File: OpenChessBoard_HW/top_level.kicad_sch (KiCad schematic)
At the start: 25 parts, among them U1 AH3572-SA-7, U2 AH3572-SA-7, U3 AH3572-SA-7, U4 AH3572-SA-7, U5 74HC4051, U6 74LVC1G79

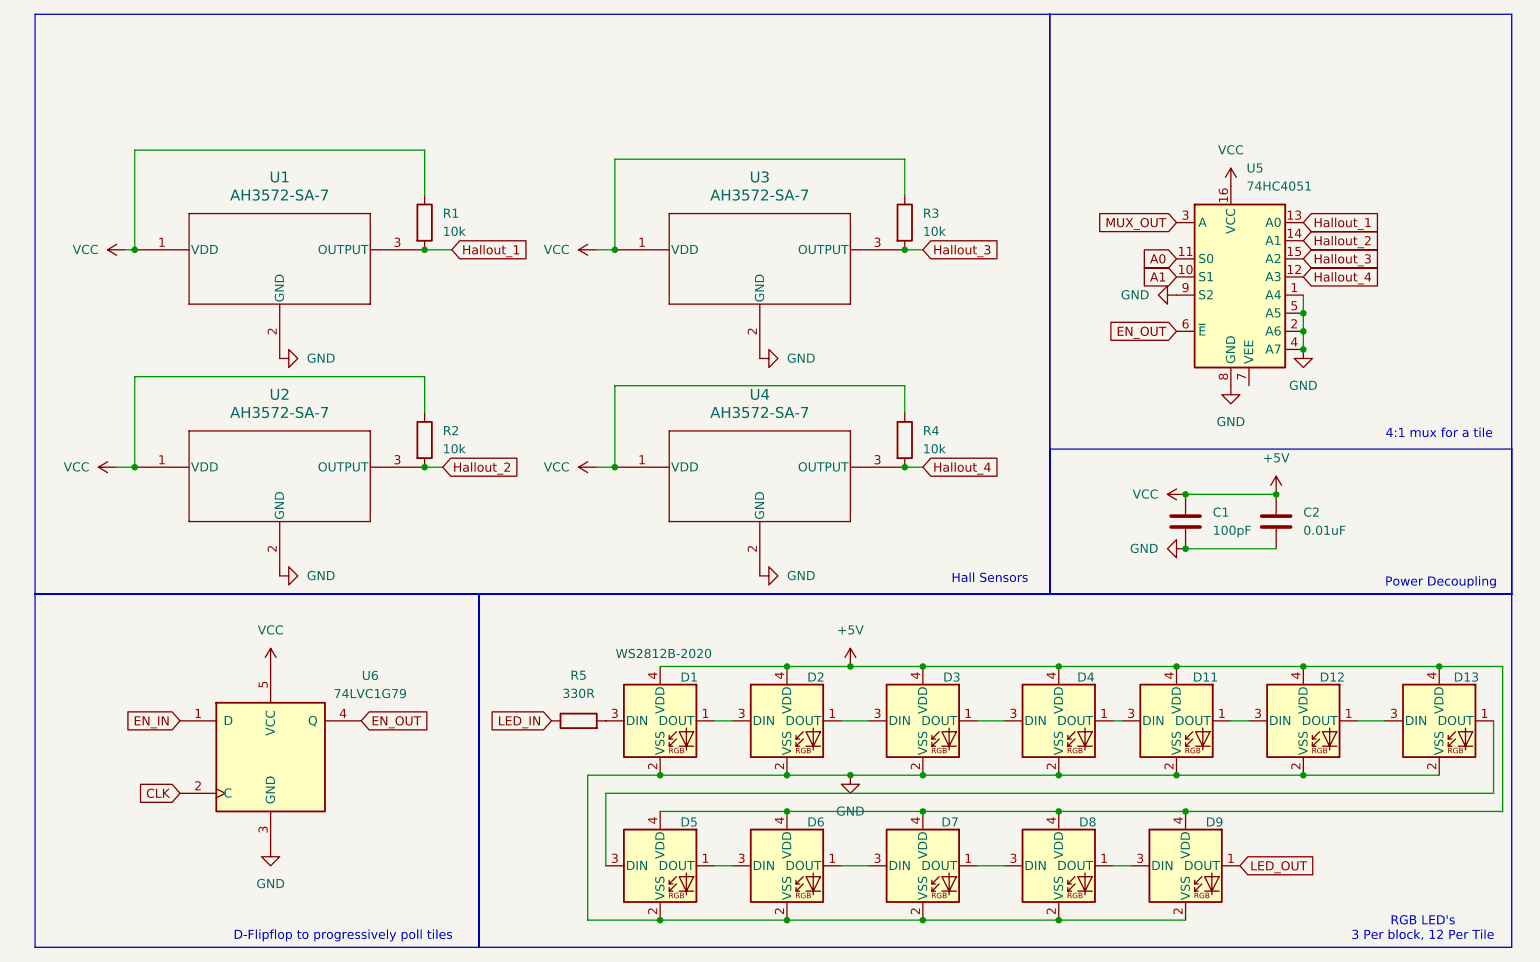
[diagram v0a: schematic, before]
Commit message: Added Basic Tile layout and Main Board
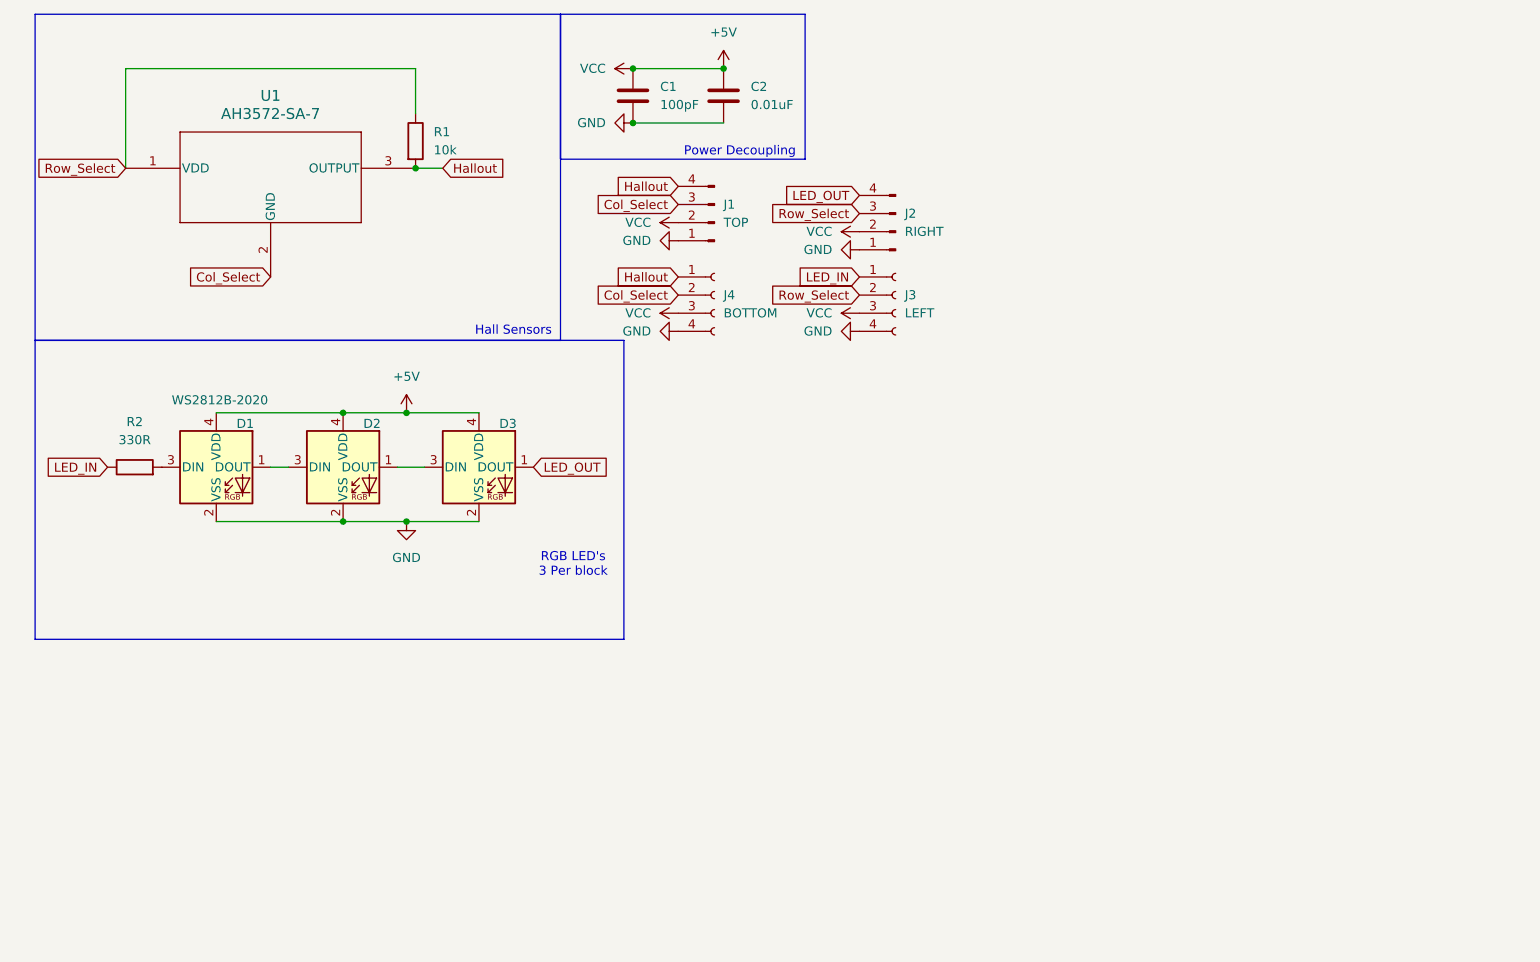
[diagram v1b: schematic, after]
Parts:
- removed D11, D12, D13, D4, D5, D6, D7, D8, D9: WS2812B-2020, LED_SMD:LED_WS2812B-2020_PLCC4_2.0x2.0mm, symbol LED:WS2812B-2020
- removed R2, R3, R4: 10k, symbol Device:R
- removed U2, U3, U4: AH3572-SA-7, SOT23_AH3572-SA-7_DIO, symbol Sensor_Magnetic:AH3572-SA-7
- removed U5: 74HC4051, symbol 74xx:74HC4051
- removed U6: 74LVC1G79, Package_SO:TSOP-5_1.65x3.05mm_P0.95mm, symbol 74xGxx:74LVC1G79
- added J1: TOP, symbol Connector:Conn_01x04_Pin
- added J2: RIGHT, symbol Connector:Conn_01x04_Pin
- added J3: LEFT, symbol Connector:Conn_01x04_Socket
- added J4: BOTTOM, symbol Connector:Conn_01x04_Socket
- C1, C2: footprint (none) -> Capacitor_SMD:C_0201_0603Metric_Pad0.64x0.40mm_HandSolder
- R1: footprint (none) -> Resistor_SMD:R_0201_0603Metric_Pad0.64x0.40mm_HandSolder
- R2: renamed from R5; footprint (none) -> Resistor_SMD:R_0201_0603Metric_Pad0.64x0.40mm_HandSolder
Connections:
- net +5V: now also J1.2 (Pin_2), J2.2 (Pin_2), J3.3 (Pin_3), J4.3 (Pin_3); no longer R1.1, U1.1 (VDD)
- net GND: now also J1.1 (Pin_1), J2.1 (Pin_1), J3.4 (Pin_4), J4.4 (Pin_4); no longer U1.2 (GND)
- net LED_IN: now also J3.1 (Pin_1)
- net LED_OUT: now also D3.1 (DOUT), J2.4 (Pin_4)
- net Hallout_1 renamed Hallout
- net Hallout: now also J1.4 (Pin_4), J4.1 (Pin_1)
- new net Col_Select: J1.3 (Pin_3), J4.2 (Pin_2), U1.2 (GND)
- new net Row_Select: J2.3 (Pin_3), J3.2 (Pin_2), R1.1, U1.1 (VDD)
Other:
- note added: "RGB LED's 3 Per block"
- note removed: "4:1 mux for a tile"
- note removed: "D-Flipflop to progressively poll tiles"
- note removed: "RGB LED's 3 Per block, 12 Per Tile"
- moved on the sheet: D1, D2, D3, R1, R2, U1
